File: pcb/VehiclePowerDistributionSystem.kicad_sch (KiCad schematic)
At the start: 30 parts, among them J1 B4B-XH-A, J2 B4B-XH-A, J3 B4B-XH-A, J4 B8B-XH-A, J5 B2B-XH-A, J6 FFC2B28-24-G, J7 B2B-XH-A, J8 B2B-XH-A, U4 D24V7F5, U5 D24V7F3, U8 BTS462TATMA1

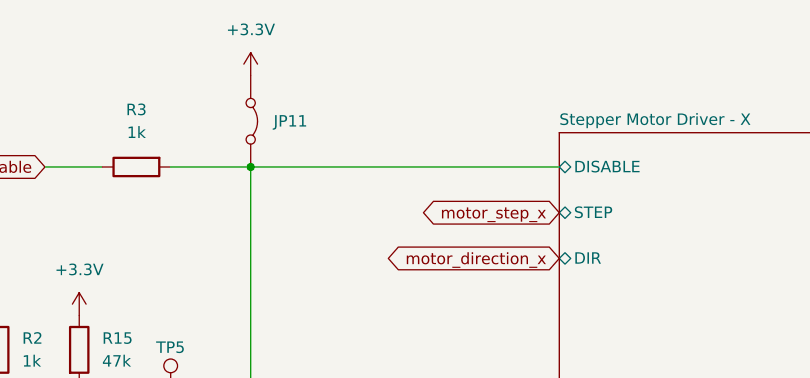
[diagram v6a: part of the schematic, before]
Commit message: Added pull-up for TMC2209 enable pins.
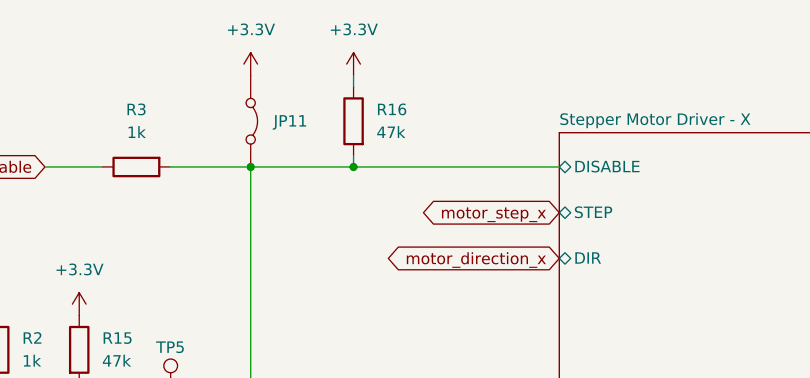
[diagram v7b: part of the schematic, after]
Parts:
- added R16: 47k, Resistor_SMD:R_1206_3216Metric_Pad1.30x1.75mm_HandSolder, symbol Device:R
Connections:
- net +3.3V: now also R16.1
- net Stepper Motor Driver - X/DISABLE: now also R16.2
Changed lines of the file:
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@@
 	)
 	(junction
+		(at 101.6 38.1)
+		(diameter 0)
+		(color 0 0 0 0)
+	)
+	(junction
 		(at 281.94 147.32)
 		(diameter 0)
@@
 	(wire
 		(pts
+			(xy 101.6 27.94) (xy 101.6 29.21)
+		)
+		(stroke
+			(width 0)
+			(type default)
+		)
+	)
+	(wire
+		(pts
 			(xy 90.17 38.1) (xy 90.17 88.9)
 		)
@@
 	(wire
 		(pts
-			(xy 90.17 38.1) (xy 124.46 38.1)
+			(xy 90.17 38.1) (xy 101.6 38.1)
 		)
 		(stroke
@@
 	(wire
 		(pts
+			(xy 101.6 36.83) (xy 101.6 38.1)
+		)
+		(stroke
+			(width 0)
+			(type default)
+		)
+	)
+	(wire
+		(pts
 			(xy 339.09 158.75) (xy 339.09 147.32)
 		)
@@
 	(wire
 		(pts
+			(xy 101.6 38.1) (xy 124.46 38.1)
+		)
+		(stroke
+			(width 0)
+			(type default)
+		)
+	)
+	(wire
+		(pts
 			(xy 62.23 63.5) (xy 71.12 63.5)
 		)
@@
 	)
 	(symbol
+		(lib_id "power:+3.3V")
+		(at 101.6 27.94 0)
+		(unit 1)
+		(exclude_from_sim no)
+		(in_bom yes)
+		(on_board yes)
+		(dnp no)
+		(fields_autoplaced yes)
+		(property "Reference" "#PWR067"
+			(at 101.6 31.75 0)
+			(effects
+				(font
+					(size 1.27 1.27)
+				)
+				(hide yes)
+			)
+		)
+		(property "Value" "+3.3V"
+			(at 101.6 22.86 0)
+			(effects
+				(font
+					(size 1.27 1.27)
+				)
+			)
+		)
+		(property "Footprint" ""
+			(at 101.6 27.94 0)
+			(effects
+				(font
+					(size 1.27 1.27)
+				)
+				(hide yes)
+			)
+		)
+		(property "Datasheet" ""
+			(at 101.6 27.94 0)
+			(effects
+				(font
+					(size 1.27 1.27)
+				)
+				(hide yes)
+			)
+		)
+		(property "Description" "Power symbol creates a global label with name \"+3.3V\""
+			(at 101.6 27.94 0)
+			(effects
+				(font
+					(size 1.27 1.27)
+				)
+				(hide yes)
+			)
+		)
+		(pin "1"
+		)
+		(instances
+			(project "VehiclePowerDistributionSystem"
+				(path "/92a7a41c-8494-4e4b-ac2d-deb1f1cd8085"
+					(reference "#PWR067")
+					(unit 1)
+				)
+			)
+		)
+	)
+	(symbol
 		(lib_id "power:GND")
 		(at 227.33 218.44 270)
@@
 					(unit 1)
 				)
+			)
+		)
+	)
+	(symbol
+		(lib_id "Device:R")
+		(at 101.6 33.02 0)
+		(mirror y)
+		(unit 1)
+		(exclude_from_sim no)
+		(in_bom yes)
+		(on_board yes)
+		(dnp no)
+		(fields_autoplaced yes)
+		(property "Reference" "R16"
+			(at 104.14 31.7499 0)
+			(effects
+				(font
+					(size 1.27 1.27)
+				)
+				(justify right)
+			)
+		)
+		(property "Value" "47k"
+			(at 104.14 34.2899 0)
+			(effects
+				(font
+					(size 1.27 1.27)
+				)
+				(justify right)
+			)
+		)
+		(property "Footprint" "Resistor_SMD:R_1206_3216Metric_Pad1.30x1.75mm_HandSolder"
+			(at 103.378 33.02 90)
+			(effects
+				(font
+					(size 1.27 1.27)
+				)
+				(hide yes)
+			)
+		)
+		(property "Datasheet" "~"
+			(at 101.6 33.02 0)
+			(effects
+				(font
+					(size 1.27 1.27)
+				)
+				(hide yes)
+			)
+		)
+		(property "Description" "Resistor"
+			(at 101.6 33.02 0)
+			(effects
+				(font
+					(size 1.27 1.27)
+				)
+				(hide yes)
+			)
+		)
+		(pin "1"
+		)
+		(pin "2"
+		)
+		(instances
+			(project "VehiclePowerDistributionSystem"
+				(path "/92a7a41c-8494-4e4b-ac2d-deb1f1cd8085"
+					(reference "R16")
+					(unit 1)
+				)

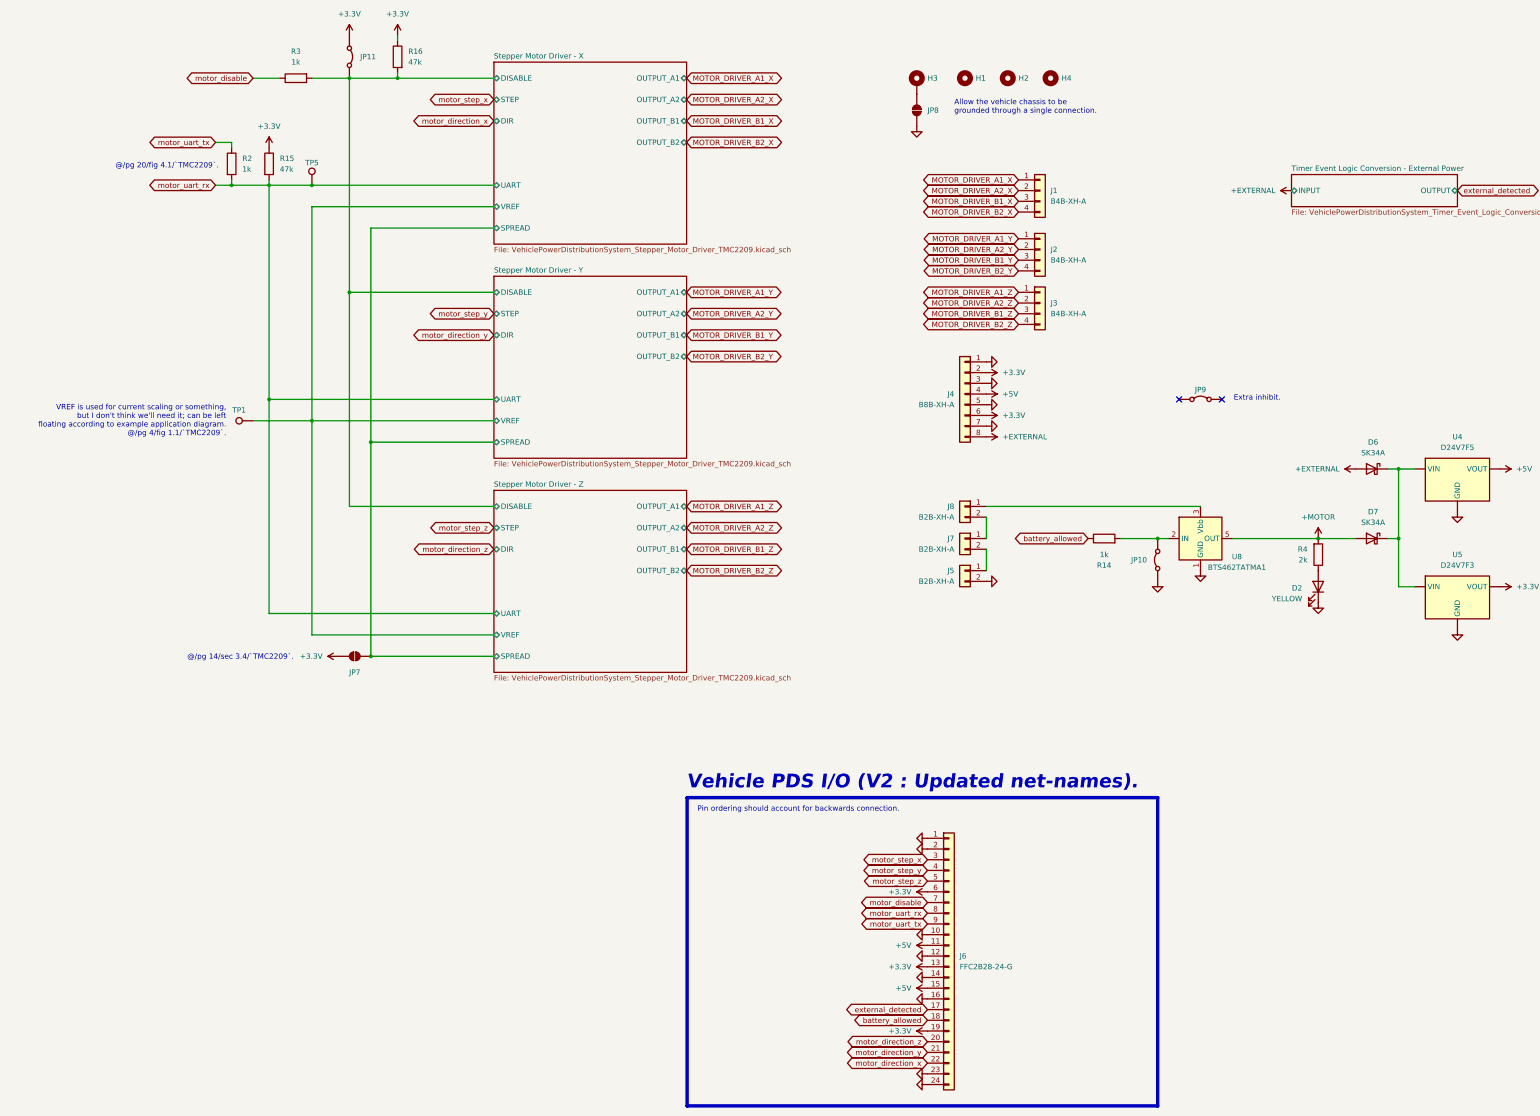
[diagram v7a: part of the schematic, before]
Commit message: Deprecated `motor_uart_rx` for `VehicleFlightComputer` and `VehiclePowerDistributionSystem`.
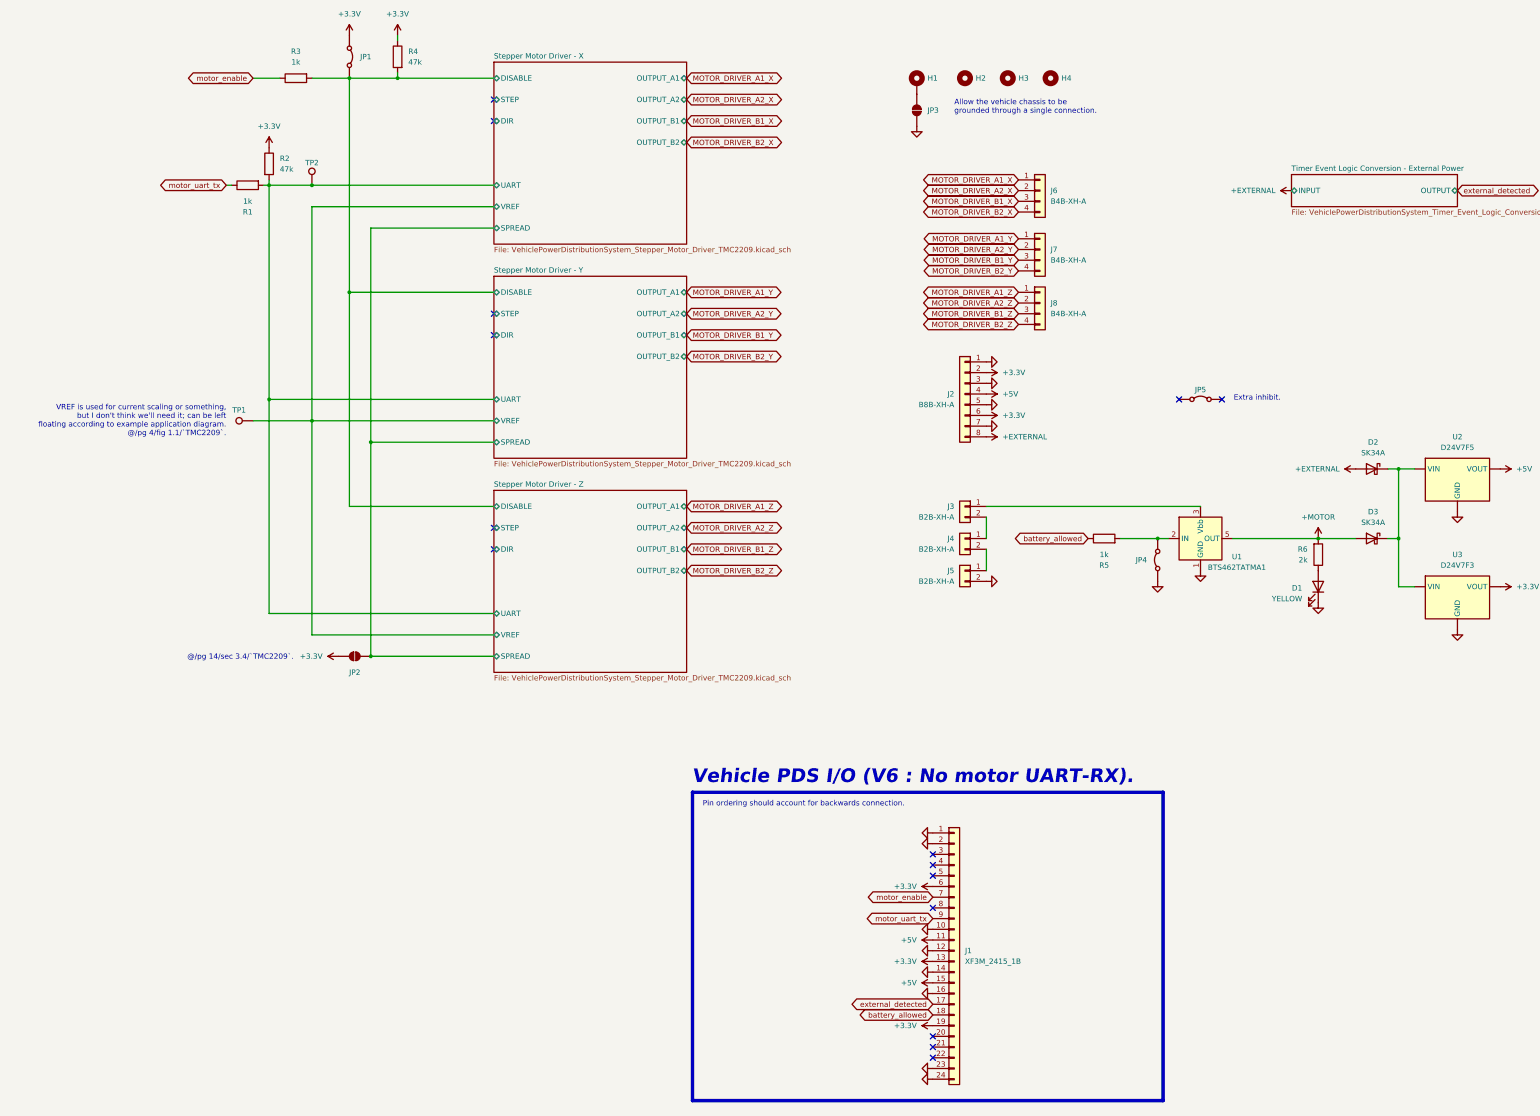
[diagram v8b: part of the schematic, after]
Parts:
- removed J6: FFC2B28-24-G, pcb:Flat Flexible Cable 24-Pin 0.5mm Connector, symbol Connector_Generic:Conn_01x24
- added J1: XF3M_2415_1B, pcb:XF3M_2415_1B, symbol Connector_Generic:Conn_01x24
- renumbered D2 to D1, D6 to D2, D7 to D3, H3 to H1, H1 to H2, H2 to H3, J4 to J2, J8 to J3, J7 to J4, J1 to J6, J2 to J7, J3 to J8, JP11 to JP1, JP7 to JP2, JP8 to JP3, JP10 to JP4, JP9 to JP5, R2 to R1, R15 to R2, R16 to R4, R14 to R5, R4 to R6, TP5 to TP2, U8 to U1, U4 to U2, U5 to U3
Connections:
- net +3.3V: now also J1.13 (Pin_13), J1.19 (Pin_19), J1.6 (Pin_6)
- net +5V: now also J1.11 (Pin_11), J1.15 (Pin_15)
- net GND: now also J1.1 (Pin_1), J1.10 (Pin_10), J1.12 (Pin_12), J1.14 (Pin_14), J1.16 (Pin_16), J1.2 (Pin_2), J1.23 (Pin_23), J1.24 (Pin_24)
- net battery_allowed: now also J1.18 (Pin_18)
- net external_detected: now also J1.17 (Pin_17)
- net motor_uart_tx: now also J1.9 (Pin_9)
- net motor_disable renamed motor_enable
- net motor_enable: now also J1.7 (Pin_7)
- net motor_uart_rx renamed Stepper Motor Driver - X/UART
- no-connect marks 2 -> 15
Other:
- note added: "Vehicle PDS I/O (V6 : No motor UART-RX)."
- note removed: "@/pg 20/fig 4.1/`TMC2209`."
- note removed: "Vehicle PDS I/O (V2 : Updated net-names)."
- moved on the sheet: R1
